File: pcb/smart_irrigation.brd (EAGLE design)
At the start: 76.2 x 76.2 mm, 33 parts, among them IC1 TMP36, IC2 7805DT, IC3 7833DT, IC4 DS1307, Q1 IRF730, Q2 32.768, T1 2N3904, U1 BL600

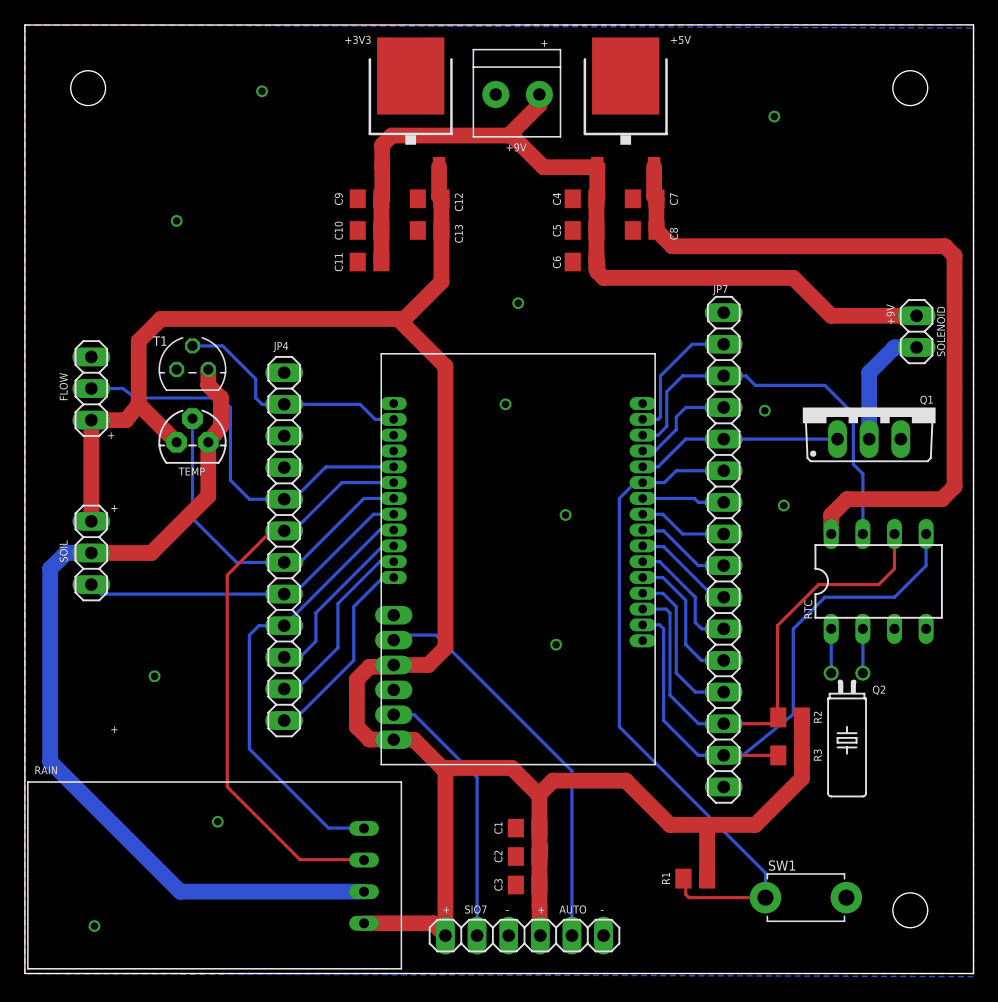
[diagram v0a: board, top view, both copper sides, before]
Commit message: PCB: Reroute SDA and RTC_DATA lines
They were precariously placed so that shorts could occur.
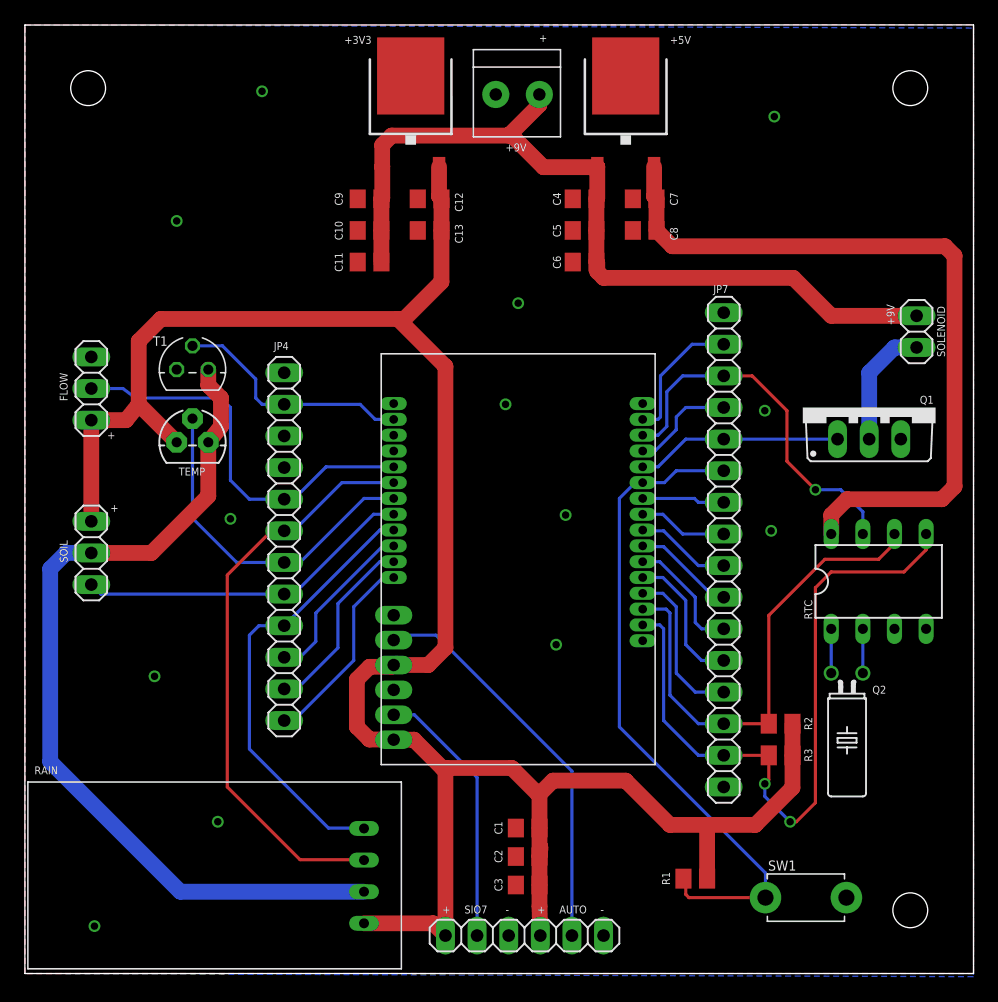
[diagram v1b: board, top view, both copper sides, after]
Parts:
- moved R2 0.92 mm to (60.7, 20.1)
- moved R3 0.76 mm to (60.7, 17.5)
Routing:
- net SDA: track 48.5 -> 56.5 mm, vias 0 -> 2
- net RTC_DATA: track 31.8 -> 30.0 mm, vias 0 -> 1
- net +3V3: track 181.3 -> 180.5 mm
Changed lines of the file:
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@@
 <text x="6.858" y="37.084" size="0.635" layer="25" font="vector" ratio="20">+</text>
 <text x="2.794" y="48.26" size="0.635" layer="25" font="vector" ratio="20" rot="R270">FLOW</text>
-<text x="6.858" y="19.304" size="0.635" layer="25" font="vector" ratio="20">+</text>
 <text x="0.762" y="16.002" size="0.635" layer="25" font="vector" ratio="20">RAIN</text>
 <text x="42.926" y="4.826" size="0.635" layer="25" font="vector" ratio="20">AUTO</text>
@@
 <text x="25.654" y="74.676" size="0.635" layer="25" font="vector" ratio="20">+3V3</text>
 <text x="51.816" y="74.676" size="0.635" layer="25" font="vector" ratio="20">+5V</text>
-<text x="41.402" y="74.422" size="0.635" layer="25" font="vector" ratio="20">+</text>
+<text x="41.3004" y="74.8284" size="0.635" layer="25" font="vector" ratio="20">+</text>
 <text x="14.478" y="40.64" size="0.635" layer="25" font="vector" ratio="20" rot="R180">TEMP</text>
 <text x="6.604" y="42.926" size="0.635" layer="25" font="vector" ratio="20">+</text>
@@
 <attribute name="NAME" x="68.072" y="22.479" size="0.635" layer="25" font="vector" ratio="20"/>
 </element>
-<element name="R3" library="rcl" package="M0805" value="2.2k" x="61.468" y="17.526" smashed="yes">
-<attribute name="NAME" x="64.008" y="17.018" size="0.635" layer="25" font="vector" ratio="20" rot="R90"/>
-</element>
-<element name="R2" library="rcl" package="M0805" value="2.2k" x="61.468" y="20.574" smashed="yes">
-<attribute name="NAME" x="64.008" y="20.066" size="0.635" layer="25" font="vector" ratio="20" rot="R90"/>
+<element name="R3" library="rcl" package="M0805" value="2.2k" x="60.706" y="17.526" smashed="yes">
+<attribute name="NAME" x="63.246" y="17.018" size="0.635" layer="25" font="vector" ratio="20" rot="R90"/>
+</element>
+<element name="R2" library="rcl" package="M0805" value="2.2k" x="60.706" y="20.066" smashed="yes">
+<attribute name="NAME" x="63.246" y="19.558" size="0.635" layer="25" font="vector" ratio="20" rot="R90"/>
 </element>
 <element name="IC1" library="smart_irrigation" package="TO92" value="TMP36" x="13.462" y="42.672" smashed="yes"/>
@@
 <contactref element="Q1" pad="S"/>
 <contactref element="T1" pad="3"/>
-<polygon width="0.254" layer="1">
+<polygon width="0.254" layer="1" isolate="0.254">
 <vertex x="0" y="76.2"/>
 <vertex x="76.2" y="76.2"/>
@@
 <vertex x="0" y="0"/>
 </polygon>
-<polygon width="0.254" layer="16">
+<polygon width="0.254" layer="16" isolate="0.254">
 <vertex x="0" y="76.2"/>
 <vertex x="76.2" y="75.946"/>
@@
 <via x="15.494" y="12.192" extent="1-16" drill="0.6"/>
 <via x="38.608" y="45.72" extent="1-16" drill="0.6"/>
-<via x="60.96" y="37.592" extent="1-16" drill="0.6"/>
+<via x="59.944" y="35.56" extent="1-16" drill="0.6"/>
 <contactref element="SW1" pad="P$2"/>
 <via x="59.436" y="45.212" extent="1-16" drill="0.6"/>
 <contactref element="IC4" pad="3"/>
+<via x="16.51" y="36.5252" extent="1-16" drill="0.6"/>
 </signal>
 <signal name="+9V">
@@
 <wire x1="33.268" y1="62.424" x2="33.462" y2="62.23" width="1.27" layer="1"/>
 <wire x1="33.462" y1="62.23" x2="33.462" y2="59.69" width="1.27" layer="1"/>
-<wire x1="62.418" y1="17.526" x2="62.418" y2="15.682" width="1.27" layer="1"/>
-<wire x1="62.418" y1="15.682" x2="58.674" y2="11.938" width="1.27" layer="1"/>
 <wire x1="58.674" y1="11.938" x2="54.864" y2="11.938" width="1.27" layer="1"/>
 <wire x1="54.864" y1="11.938" x2="51.816" y2="11.938" width="1.27" layer="1"/>
 <wire x1="51.816" y1="11.938" x2="48.26" y2="15.494" width="1.27" layer="1"/>
-<wire x1="62.418" y1="17.526" x2="62.418" y2="20.574" width="1.27" layer="1"/>
 <wire x1="29.836" y1="24.892" x2="29.624" y2="24.782" width="1.27" layer="16"/>
 <wire x1="33.462" y1="59.69" x2="33.462" y2="55.56" width="1.27" layer="1"/>
@@
 <wire x1="32.798" y1="4.032" x2="33.782" y2="3.048" width="1.27" layer="1"/>
 <wire x1="33.782" y1="3.048" x2="33.782" y2="16.51" width="1.27" layer="1"/>
+<wire x1="58.674" y1="11.938" x2="61.656" y2="14.92" width="1.27" layer="1"/>
+<wire x1="61.656" y1="14.92" x2="61.656" y2="17.526" width="1.27" layer="1"/>
+<wire x1="61.656" y1="17.526" x2="61.656" y2="20.066" width="1.27" layer="1"/>
 </signal>
 <signal name="NAUTORUN">
@@
 <contactref element="JP7" pad="3"/>
 <contactref element="IC4" pad="7"/>
-<wire x1="67.31" y1="35.306" x2="67.31" y2="40.132" width="0.254" layer="16"/>
-<wire x1="67.31" y1="40.132" x2="66.548" y2="40.894" width="0.254" layer="16"/>
-<wire x1="66.548" y1="40.894" x2="66.548" y2="44.958" width="0.254" layer="16"/>
-<wire x1="66.548" y1="44.958" x2="64.262" y2="47.244" width="0.254" layer="16"/>
-<wire x1="64.262" y1="47.244" x2="58.674" y2="47.244" width="0.254" layer="16"/>
-<wire x1="58.674" y1="47.244" x2="57.912" y2="48.006" width="0.254" layer="16"/>
-<wire x1="57.912" y1="48.006" x2="56.134" y2="48.006" width="0.254" layer="16"/>
 <wire x1="49.624" y1="43.242" x2="50.862" y2="43.242" width="0.254" layer="16"/>
 <wire x1="50.862" y1="43.242" x2="51.562" y2="43.942" width="0.254" layer="16"/>
@@
 <wire x1="51.562" y1="46.736" x2="52.832" y2="48.006" width="0.254" layer="16"/>
 <wire x1="52.832" y1="48.006" x2="56.134" y2="48.006" width="0.254" layer="16"/>
+<wire x1="56.134" y1="48.006" x2="58.42" y2="48.006" width="0.254" layer="1"/>
+<wire x1="58.42" y1="48.006" x2="61.214" y2="45.212" width="0.254" layer="1"/>
+<wire x1="61.214" y1="45.212" x2="61.214" y2="41.148" width="0.254" layer="1"/>
+<wire x1="61.214" y1="41.148" x2="63.5" y2="38.862" width="0.254" layer="1"/>
+<via x="63.5" y="38.862" extent="1-16" drill="0.6"/>
+<wire x1="63.5" y1="38.862" x2="65.532" y2="38.862" width="0.254" layer="16"/>
+<wire x1="65.532" y1="38.862" x2="67.31" y2="37.084" width="0.254" layer="16"/>
+<wire x1="67.31" y1="37.084" x2="67.31" y2="35.306" width="0.254" layer="16"/>
 </signal>
 <signal name="SOL_ENABLE">
@@
 <contactref element="IC4" pad="6"/>
 <contactref element="R2" pad="1"/>
-<wire x1="69.85" y1="35.306" x2="69.85" y2="32.512" width="0.254" layer="1"/>
-<wire x1="69.85" y1="32.512" x2="68.58" y2="31.242" width="0.254" layer="1"/>
-<wire x1="68.58" y1="31.242" x2="63.754" y2="31.242" width="0.254" layer="1"/>
-<wire x1="63.754" y1="31.242" x2="60.452" y2="27.94" width="0.254" layer="1"/>
-<wire x1="60.452" y1="27.94" x2="60.452" y2="20.64" width="0.254" layer="1"/>
-<wire x1="60.452" y1="20.64" x2="60.518" y2="20.574" width="0.254" layer="1"/>
-<wire x1="60.518" y1="20.574" x2="60.01" y2="20.066" width="0.254" layer="1"/>
-<wire x1="60.01" y1="20.066" x2="56.134" y2="20.066" width="0.254" layer="1"/>
 <wire x1="49.624" y1="29.272" x2="51.5" y2="29.272" width="0.254" layer="16"/>
 <wire x1="51.5" y1="29.272" x2="51.816" y2="28.956" width="0.254" layer="16"/>
@@
 <wire x1="51.816" y1="22.352" x2="54.102" y2="20.066" width="0.254" layer="16"/>
 <wire x1="54.102" y1="20.066" x2="56.134" y2="20.066" width="0.254" layer="16"/>
+<wire x1="69.85" y1="35.4584" x2="69.85" y2="35.306" width="0.254" layer="1"/>
+<wire x1="69.85" y1="35.306" x2="69.85" y2="34.544" width="0.254" layer="1"/>
+<wire x1="69.85" y1="34.544" x2="68.58" y2="33.274" width="0.254" layer="1"/>
+<wire x1="68.58" y1="33.274" x2="64.262" y2="33.274" width="0.254" layer="1"/>
+<wire x1="59.756" y1="20.066" x2="56.134" y2="20.066" width="0.254" layer="1"/>
+<wire x1="59.756" y1="20.066" x2="59.756" y2="28.768" width="0.254" layer="1"/>
+<wire x1="59.756" y1="28.768" x2="64.262" y2="33.274" width="0.254" layer="1"/>
 </signal>
 <signal name="SDA">
@@
 <contactref element="IC4" pad="5"/>
 <contactref element="R3" pad="1"/>
-<wire x1="60.518" y1="17.526" x2="56.134" y2="17.526" width="0.254" layer="1"/>
-<wire x1="72.39" y1="35.306" x2="72.39" y2="32.766" width="0.254" layer="16"/>
-<wire x1="72.39" y1="32.766" x2="69.85" y2="30.226" width="0.254" layer="16"/>
-<wire x1="69.85" y1="30.226" x2="64.262" y2="30.226" width="0.254" layer="16"/>
-<wire x1="64.262" y1="30.226" x2="61.722" y2="27.686" width="0.254" layer="16"/>
-<wire x1="61.722" y1="27.686" x2="61.722" y2="20.828" width="0.254" layer="16"/>
-<wire x1="56.134" y1="17.526" x2="57.658" y2="17.526" width="0.254" layer="16"/>
-<wire x1="57.658" y1="17.526" x2="61.722" y2="20.828" width="0.254" layer="16"/>
 <wire x1="49.624" y1="28.002" x2="50.992" y2="28.002" width="0.254" layer="16"/>
 <wire x1="50.992" y1="28.002" x2="51.308" y2="27.686" width="0.254" layer="16"/>
@@
 <wire x1="51.308" y1="20.32" x2="54.102" y2="17.526" width="0.254" layer="16"/>
 <wire x1="54.102" y1="17.526" x2="56.134" y2="17.526" width="0.254" layer="16"/>
+<wire x1="59.756" y1="17.526" x2="56.134" y2="17.526" width="0.254" layer="1"/>
+<wire x1="59.756" y1="17.526" x2="59.756" y2="15.56" width="0.254" layer="1"/>
+<wire x1="59.756" y1="15.56" x2="59.436" y2="15.24" width="0.254" layer="1"/>
+<via x="59.436" y="15.24" extent="1-16" drill="0.6"/>
+<wire x1="59.436" y1="15.24" x2="59.436" y2="14.224" width="0.254" layer="16"/>
+<wire x1="59.436" y1="14.224" x2="61.468" y2="12.192" width="0.254" layer="16"/>
+<via x="61.468" y="12.192" extent="1-16" drill="0.6"/>
+<wire x1="61.468" y1="12.192" x2="61.976" y2="12.192" width="0.254" layer="1"/>
+<wire x1="61.976" y1="12.192" x2="63.5" y2="13.716" width="0.254" layer="1"/>
+<wire x1="63.5" y1="13.716" x2="63.5" y2="30.988" width="0.254" layer="1"/>
+<wire x1="63.5" y1="30.988" x2="64.77" y2="32.258" width="0.254" layer="1"/>
+<wire x1="64.77" y1="32.258" x2="70.612" y2="32.258" width="0.254" layer="1"/>
+<wire x1="70.612" y1="32.258" x2="72.39" y2="34.036" width="0.254" layer="1"/>
+<wire x1="72.39" y1="34.036" x2="72.39" y2="35.306" width="0.254" layer="1"/>
 </signal>
 <signal name="SOL_DRAIN">

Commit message: PCB: Rename RTC_DATA to RTC_SQW
The signal is actually a square wave, not any sort of data.
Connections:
- net RTC_DATA renamed RTC_SQW
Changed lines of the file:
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@@
 <wire x1="53.594" y1="50.546" x2="56.134" y2="50.546" width="0.254" layer="16"/>
 </signal>
-<signal name="RTC_DATA">
+<signal name="RTC_SQW">
 <contactref element="U1" pad="26"/>
 <contactref element="JP7" pad="3"/>
